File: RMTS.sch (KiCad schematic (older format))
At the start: 54 parts, among them J1 USB_B, J10 CONN_02, J2 Programmer, J3 Screw_Terminal_01x03, J4 Screw_Terminal_01x04, J5 Screw_Terminal_01x02, J6 Screw_Terminal_01x02, J7 Micro_SD_Card_Det_Hirose_DM3AT, J8 CONN_03, J9 CONN_02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

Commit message: Added continuity optocoupler, capacitor pads to loadcell connection
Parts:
- added C17: 0.47uF, Capacitor_SMD:C_0805_2012Metric_Pad1.15x1.40mm_HandSolder, symbol Device:C
- added R11, R12: 500, Resistor_SMD:R_0805_2012Metric_Pad1.15x1.40mm_HandSolder, symbol Device:R_US
- added U5: LTV-817S, Package_DIP:SMDIP-4_W9.53mm, symbol Isolator:LTV-817S
- J10, J9: symbol RMTS-rescue:CONN_02-SparkFun-Connectors -> RMTS-rescue:CONN_02-SparkFun-Connectors-RMTS-rescue
- J8: symbol RMTS-rescue:CONN_03-SparkFun-Connectors -> RMTS-rescue:CONN_03-SparkFun-Connectors-RMTS-rescue
- JP1: symbol RMTS-rescue:XBEE-SparkFun-RF -> RMTS-rescue:XBEE-SparkFun-RF-RMTS-rescue
- U2: symbol RMTS-rescue:MK20DX256VLH7-Mine -> RMTS-rescue:MK20DX256VLH7-Mine-RMTS-rescue
- U3: symbol RMTS-rescue:ADS1219-Mine -> RMTS-rescue:ADS1219-Mine-RMTS-rescue
- U4: symbol RMTS-rescue:MCP6N11-Mine -> RMTS-rescue:MCP6N11-Mine-RMTS-rescue
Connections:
- net labels added: CONT
- wire segments 197 -> 206
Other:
- moved on the sheet: D1, D3, J5, J6, Q1, R9

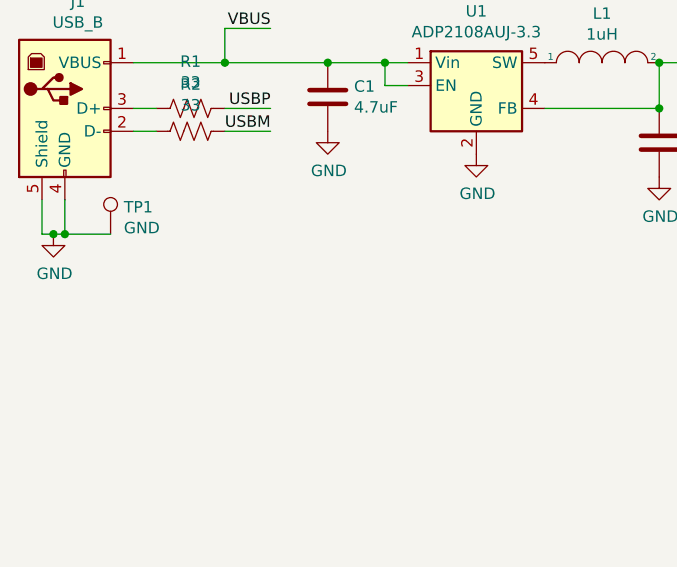
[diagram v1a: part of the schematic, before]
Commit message: Added resistor to avoid battery shutting off
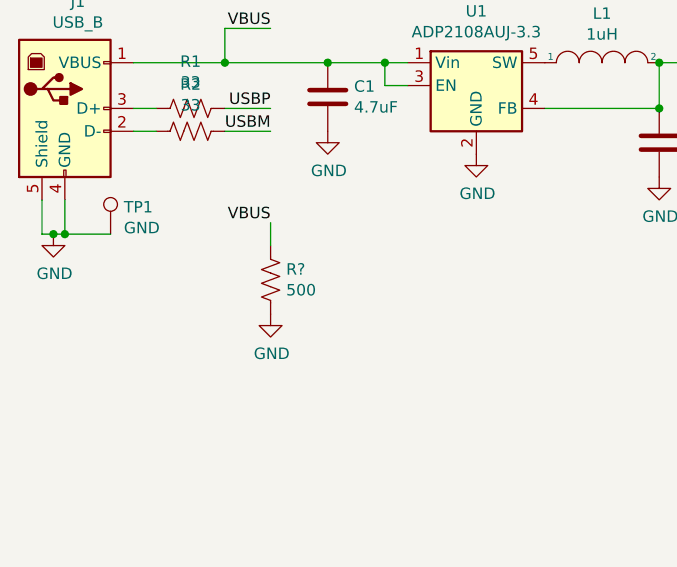
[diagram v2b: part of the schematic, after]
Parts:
- added R?: 500, symbol Device:R_US
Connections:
- net GND: now also R?.2
- net VBUS: now also R?.1
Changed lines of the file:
@@
 Wire Wire Line
 	14100 6600 14400 6600
+$Comp
+L Device:R_US R?
+U 1 1 5E3F0EC8
+P 1900 2200
+F 0 "R?" H 1968 2246 50  0000 L CNN
+F 1 "500" H 1968 2155 50  0000 L CNN
+F 2 "" V 1940 2190 50  0001 C CNN
+F 3 "~" H 1900 2200 50  0001 C CNN
+	1    1900 2200
+	1    0    0    -1
+$EndComp
+$Comp
+L power:GND #PWR?
+U 1 1 5E3F4010
+P 1900 2350
+F 0 "#PWR?" H 1900 2100 50  0001 C CNN
+F 1 "GND" H 1905 2177 50  0000 C CNN
+F 2 "" H 1900 2350 50  0001 C CNN
+F 3 "" H 1900 2350 50  0001 C CNN
+	1    1900 2350
+	1    0    0    -1
+$EndComp
+Text Label 1900 1950 2    50   ~ 0
+VBUS
+Wire Wire Line
+	1900 1950 1900 2050
 $EndSCHEMATC

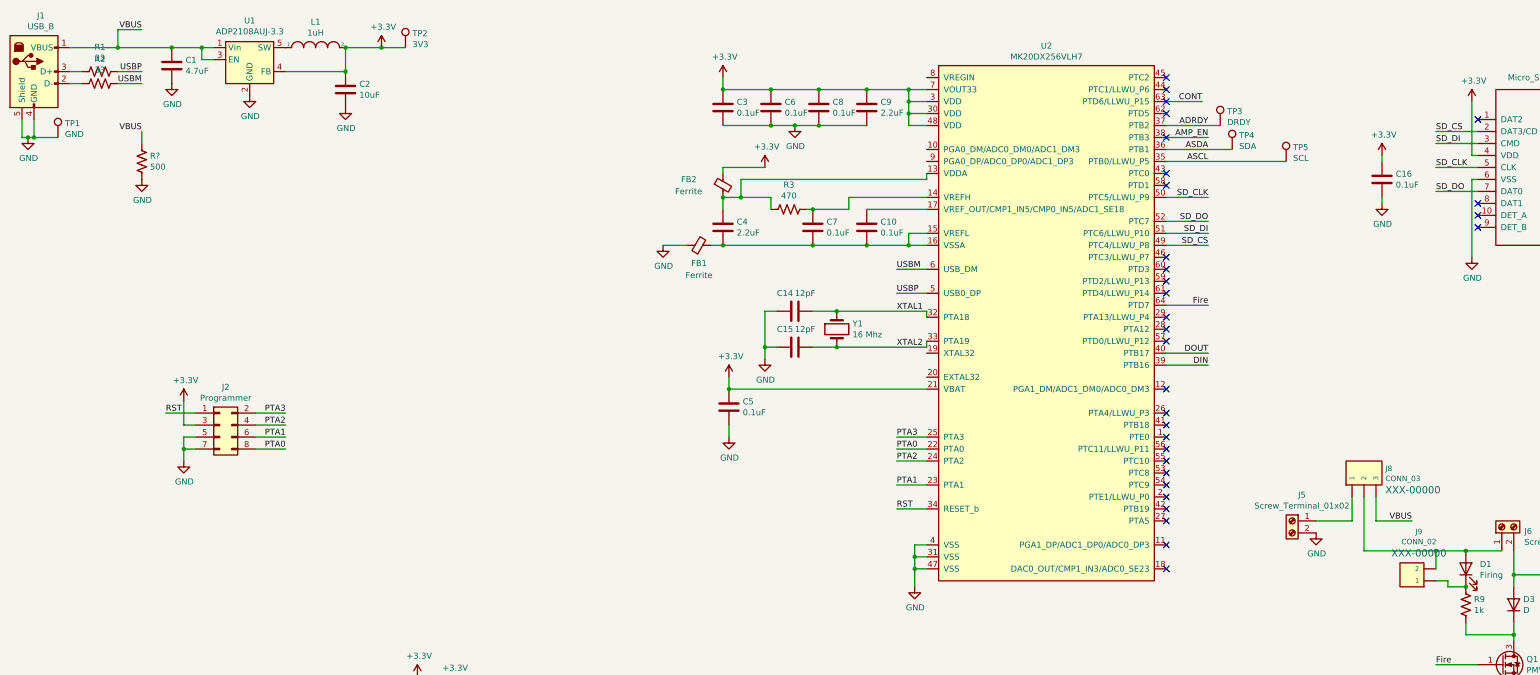
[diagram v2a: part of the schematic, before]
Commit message: Removed USB pyro power jumper
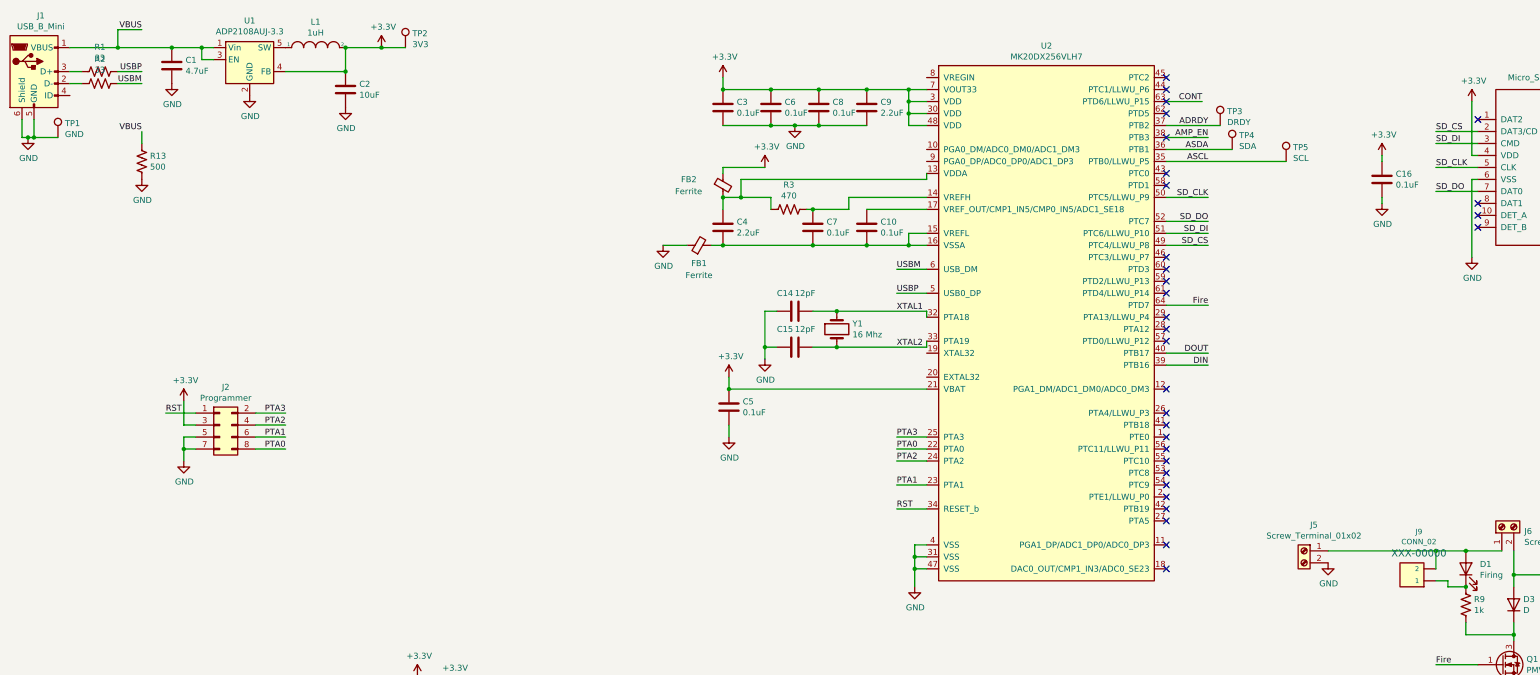
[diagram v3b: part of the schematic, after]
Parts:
- removed J1: USB_B, Connector_USB:USB_B_OST_USB-B1HSxx_Horizontal, symbol Connector:USB_B
- removed J8: CONN_03, Connectors:1X03, symbol RMTS-rescue:CONN_03-SparkFun-Connectors-RMTS-rescue
- added J1: USB_B_Mini, Connector_USB:USB_Mini-B_Lumberg_2486_01_Horizontal, symbol Connector:USB_B_Mini
- R13: renamed from R?; footprint (none) -> Resistor_SMD:R_0805_2012Metric_Pad1.15x1.40mm_HandSolder
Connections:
- net GND: now also J1.5 (GND), J1.6 (Shield)
- net VBUS: now also J1.1 (VBUS)
- net at R1.2: now also J1.3 (D+)
- net at R2.2: now also J1.2 (D-)
- net at D1.2 (A), J6.1 (Pin_1), J9.2: now also J5.1 (Pin_1)
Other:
- moved on the sheet: J5
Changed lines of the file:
@@
 Wire Wire Line
 	13250 5450 12950 5450
-Text Label 12500 5200 2    50   ~ 0
-VBUS
 $Comp
 L Device:LED D2
@@
 L Connector:Screw_Terminal_01x02 J5
 U 1 1 5D6E654F
-P 11500 5200
-F 0 "J5" H 11418 5417 50  0000 C CNN
-F 1 "Screw_Terminal_01x02" H 11418 5326 50  0000 C CNN
-F 2 "Connectors:SCREWTERMINAL-3.5MM-2" H 11500 5200 50  0001 C CNN
-F 3 "~" H 11500 5200 50  0001 C CNN
-	1    11500 5200
+P 11600 5450
+F 0 "J5" H 11518 5667 50  0000 C CNN
+F 1 "Screw_Terminal_01x02" H 11518 5576 50  0000 C CNN
+F 2 "Connectors:SCREWTERMINAL-3.5MM-2" H 11600 5450 50  0001 C CNN
+F 3 "~" H 11600 5450 50  0001 C CNN
+	1    11600 5450
 	-1   0    0    -1
 $EndComp
@@
 L power:GND #PWR0136
 U 1 1 5D6EF1A3
-P 11700 5300
-F 0 "#PWR0136" H 11700 5050 50  0001 C CNN
-F 1 "GND" H 11705 5127 50  0000 C CNN
-F 2 "" H 11700 5300 50  0001 C CNN
-F 3 "" H 11700 5300 50  0001 C CNN
-	1    11700 5300
-	1    0    0    -1
-$EndComp
-$Comp
-L RMTS-rescue:CONN_03-SparkFun-Connectors-RMTS-rescue J8
-U 1 1 5D6FAE37
-P 12000 4900
-F 0 "J8" V 11863 5178 45  0000 L CNN
-F 1 "CONN_03" V 11947 5178 45  0000 L CNN
-F 2 "Connectors:1X03" H 12000 5300 20  0001 C CNN
-F 3 "" H 12000 4900 50  0001 C CNN
-F 4 "XXX-00000" V 12042 5178 60  0000 L CNN "Field4"
-	1    12000 4900
-	0    1    1    0
-$EndComp
-Wire Wire Line
-	12100 5000 12100 5450
-Wire Wire Line
-	12100 5450 12700 5450
-Wire Wire Line
-	12200 5000 12200 5200
-Wire Wire Line
-	12200 5200 12500 5200
-Wire Wire Line
-	11700 5200 12000 5200
-Wire Wire Line
-	12000 5200 12000 5000
+P 11800 5550
+F 0 "#PWR0136" H 11800 5300 50  0001 C CNN
+F 1 "GND" H 11805 5377 50  0000 C CNN
+F 2 "" H 11800 5550 50  0001 C CNN
+F 3 "" H 11800 5550 50  0001 C CNN
+	1    11800 5550
+	1    0    0    -1
+$EndComp
 $Comp
 L Device:C C14
@@
 AMP_EN
 $Comp
-L Connector:USB_B J1
-U 1 1 5D732327
-P 1000 1450
-F 0 "J1" H 1057 1917 50  0000 C CNN
-F 1 "USB_B" H 1057 1826 50  0000 C CNN
-F 2 "Connector_USB:USB_B_OST_USB-B1HSxx_Horizontal" H 1150 1400 50  0001 C CNN
-F 3 " ~" H 1150 1400 50  0001 C CNN
-	1    1000 1450
-	1    0    0    -1
-$EndComp
-$Comp
 L Connector:TestPoint TP3
 U 1 1 5D79BB5E
@@
 	14100 6600 14400 6600
 $Comp
-L Device:R_US R?
+L Device:R_US R13
 U 1 1 5E3F0EC8
 P 1900 2200
-F 0 "R?" H 1968 2246 50  0000 L CNN
+F 0 "R13" H 1968 2246 50  0000 L CNN
 F 1 "500" H 1968 2155 50  0000 L CNN
-F 2 "" V 1940 2190 50  0001 C CNN
+F 2 "Resistor_SMD:R_0805_2012Metric_Pad1.15x1.40mm_HandSolder" V 1940 2190 50  0001 C CNN
 F 3 "~" H 1900 2200 50  0001 C CNN
 	1    1900 2200
@@
 $EndComp
 $Comp
-L power:GND #PWR?
+L power:GND #PWR0145
 U 1 1 5E3F4010
 P 1900 2350
-F 0 "#PWR?" H 1900 2100 50  0001 C CNN
+F 0 "#PWR0145" H 1900 2100 50  0001 C CNN
 F 1 "GND" H 1905 2177 50  0000 C CNN
 F 2 "" H 1900 2350 50  0001 C CNN
@@
 Wire Wire Line
 	1900 1950 1900 2050
+$Comp
+L Connector:USB_B_Mini J1
+U 1 1 5E40F3F8
+P 1000 1450
+F 0 "J1" H 1057 1917 50  0000 C CNN
+F 1 "USB_B_Mini" H 1057 1826 50  0000 C CNN
+F 2 "Connector_USB:USB_Mini-B_Lumberg_2486_01_Horizontal" H 1150 1400 50  0001 C CNN
+F 3 "~" H 1150 1400 50  0001 C CNN
+	1    1000 1450
+	1    0    0    -1
+$EndComp
+Wire Wire Line
+	11800 5450 12700 5450
 $EndSCHEMATC

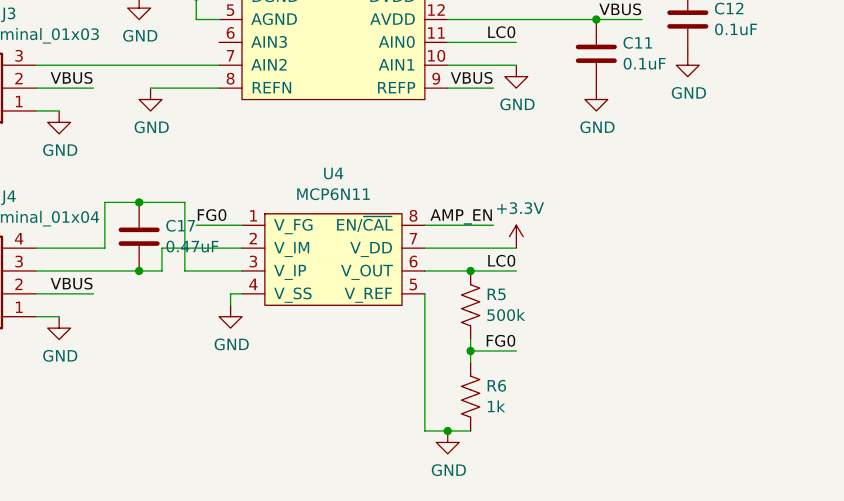
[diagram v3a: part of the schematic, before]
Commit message: Updated amplifier to MCP6N16, incremented revision number
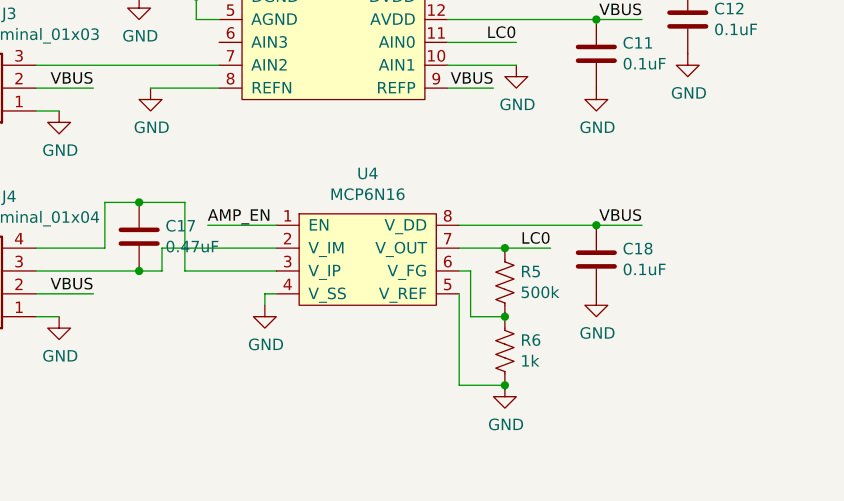
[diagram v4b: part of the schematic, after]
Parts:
- removed U4: MCP6N11, Package_SO:SOIC-8_3.9x4.9mm_P1.27mm, symbol RMTS-rescue:MCP6N11-Mine-RMTS-rescue
- added C18: 0.1uF, Capacitor_SMD:C_0805_2012Metric_Pad1.15x1.40mm_HandSolder, symbol Device:C
- added U4: MCP6N16, Package_SO:MSOP-8_3x3mm_P0.65mm, symbol Mine:MCP6N16
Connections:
- net AMP_EN: now also U4.1 (EN)
- net GND: now also C18.2, U4.4 (V_SS), U4.5 (V_REF)
- net LC0: now also U4.7 (V_OUT)
- net VBUS: now also C18.1, U4.8 (V_DD)
- net at C17.2, J4.3 (Pin_3): now also U4.2 (V_IM)
- net at C17.1, J4.4 (Pin_4): now also U4.3 (V_IP)
- net FG0: no longer names the net of R5.2, R6.1
- net FG0: now also U4.6 (V_FG)
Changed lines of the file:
@@
 	-1   0    0    1
-$EndComp
-$Comp
-L RMTS-rescue:MCP6N11-Mine-RMTS-rescue U4
-U 1 1 5D4392E2
-P 3650 8100
-F 0 "U4" H 3650 8325 50  0000 C CNN
-F 1 "MCP6N11" H 3650 8234 50  0000 C CNN
-F 2 "Package_SO:SOIC-8_3.9x4.9mm_P1.27mm" H 3650 8100 50  0001 C CNN
-F 3 "" H 3650 8100 50  0001 C CNN
-	1    3650 8100
-	1    0    0    -1
 $EndComp
 Wire Wire Line
@@
 VBUS
 Wire Wire Line
-	4050 8200 4450 8200
-Text Label 4350 8100 2    50   ~ 0
-AMP_EN
-Wire Wire Line
-	4050 8100 4350 8100
-Wire Wire Line
-	3250 8400 3200 8400
-$Comp
-L power:GND #PWR0124
-U 1 1 5D49EC97
-P 3200 8450
-F 0 "#PWR0124" H 3200 8200 50  0001 C CNN
-F 1 "GND" H 3205 8277 50  0000 C CNN
-F 2 "" H 3200 8450 50  0001 C CNN
-F 3 "" H 3200 8450 50  0001 C CNN
-	1    3200 8450
-	1    0    0    -1
-$EndComp
-Wire Wire Line
-	3200 8400 3200 8450
-$Comp
-L power:+3.3V #PWR0125
-U 1 1 5D4AF785
-P 4450 8200
-F 0 "#PWR0125" H 4450 8050 50  0001 C CNN
-F 1 "+3.3V" H 4465 8373 50  0000 C CNN
-F 2 "" H 4450 8200 50  0001 C CNN
-F 3 "" H 4450 8200 50  0001 C CNN
-	1    4450 8200
-	1    0    0    -1
-$EndComp
-Text Label 4450 8300 2    50   ~ 0
-LC0
-$Comp
-L Device:R_US R5
-U 1 1 5D4C0410
-P 4250 8450
-F 0 "R5" H 4318 8496 50  0000 L CNN
-F 1 "500k" H 4318 8405 50  0000 L CNN
-F 2 "Resistor_SMD:R_0805_2012Metric_Pad1.15x1.40mm_HandSolder" V 4290 8440 50  0001 C CNN
-F 3 "~" H 4250 8450 50  0001 C CNN
-	1    4250 8450
-	1    0    0    -1
-$EndComp
-$Comp
-L Device:R_US R6
-U 1 1 5D4C1180
-P 4250 8850
-F 0 "R6" H 4318 8896 50  0000 L CNN
-F 1 "1k" H 4318 8805 50  0000 L CNN
-F 2 "Resistor_SMD:R_0805_2012Metric_Pad1.15x1.40mm_HandSolder" V 4290 8840 50  0001 C CNN
-F 3 "~" H 4250 8850 50  0001 C CNN
-	1    4250 8850
-	1    0    0    -1
-$EndComp
-Wire Wire Line
-	4250 8600 4250 8650
-Connection ~ 4250 8650
-Wire Wire Line
-	4250 8650 4250 8700
-Wire Wire Line
-	4050 8400 4050 9000
-Wire Wire Line
-	4050 9000 4150 9000
-Wire Wire Line
-	4250 8650 4450 8650
-Text Label 4450 8650 2    50   ~ 0
-FG0
-Wire Wire Line
-	3250 8100 3050 8100
-Text Label 3050 8100 0    50   ~ 0
-FG0
-Wire Wire Line
 	4150 7300 4450 7300
 Text Label 4450 7300 2    50   ~ 0
 LC0
-$Comp
-L power:GND #PWR0126
-U 1 1 5D52CDAD
-P 4150 9000
-F 0 "#PWR0126" H 4150 8750 50  0001 C CNN
-F 1 "GND" H 4155 8827 50  0000 C CNN
-F 2 "" H 4150 9000 50  0001 C CNN
-F 3 "" H 4150 9000 50  0001 C CNN
-	1    4150 9000
-	1    0    0    -1
-$EndComp
-Connection ~ 4150 9000
-Wire Wire Line
-	4150 9000 4250 9000
 Wire Wire Line
 	4150 7400 4450 7400
@@
 Text Label 12700 2450 0    50   ~ 0
 SD_DO
-Wire Wire Line
-	4050 8300 4250 8300
-Connection ~ 4250 8300
-Wire Wire Line
-	4250 8300 4450 8300
 $Comp
 L power:GND #PWR0133
@@
 Wire Wire Line
 	3000 8000 3000 8300
-Wire Wire Line
-	3000 8300 3250 8300
 Connection ~ 2800 8000
 Wire Wire Line
@@
 Wire Wire Line
 	2900 8300 2900 8200
-Wire Wire Line
-	2900 8200 3250 8200
 Connection ~ 2800 8300
 $Comp
@@
 Wire Wire Line
 	11800 5450 12700 5450
+Wire Wire Line
+	4400 8200 4600 8200
+Connection ~ 4400 8200
+Text Label 4600 8200 2    50   ~ 0
+LC0
+Wire Wire Line
+	4200 8200 4400 8200
+Connection ~ 4400 8500
+Wire Wire Line
+	4250 8300 4200 8300
+Wire Wire Line
+	4250 8500 4250 8300
+Wire Wire Line
+	4400 8500 4250 8500
+$Comp
+L Device:R_US R6
+U 1 1 5E5AA280
+P 4400 8650
+F 0 "R6" H 4468 8696 50  0000 L CNN
+F 1 "1k" H 4468 8605 50  0000 L CNN
+F 2 "Resistor_SMD:R_0805_2012Metric_Pad1.15x1.40mm_HandSolder" V 4440 8640 50  0001 C CNN
+F 3 "~" H 4400 8650 50  0001 C CNN
+	1    4400 8650
+	1    0    0    -1
+$EndComp
+$Comp
+L Device:R_US R5
+U 1 1 5E5A9716
+P 4400 8350
+F 0 "R5" H 4468 8396 50  0000 L CNN
+F 1 "500k" H 4468 8305 50  0000 L CNN
+F 2 "Resistor_SMD:R_0805_2012Metric_Pad1.15x1.40mm_HandSolder" V 4440 8340 50  0001 C CNN
+F 3 "~" H 4400 8350 50  0001 C CNN
+	1    4400 8350
+	1    0    0    -1
+$EndComp
+$Comp
+L power:GND #PWR0124
+U 1 1 5E59AFE5
+P 4400 8800
+F 0 "#PWR0124" H 4400 8550 50  0001 C CNN
+F 1 "GND" H 4405 8627 50  0000 C CNN
+F 2 "" H 4400 8800 50  0001 C CNN
+F 3 "" H 4400 8800 50  0001 C CNN
+	1    4400 8800
+	1    0    0    -1
+$EndComp
+Wire Wire Line
+	3350 8400 3350 8450
+Wire Wire Line
+	3400 8400 3350 8400
+$Comp
+L power:GND #PWR0125
+U 1 1 5E58C5CA
+P 3350 8450
+F 0 "#PWR0125" H 3350 8200 50  0001 C CNN
+F 1 "GND" H 3355 8277 50  0000 C CNN
+F 2 "" H 3350 8450 50  0001 C CNN
+F 3 "" H 3350 8450 50  0001 C CNN
+	1    3350 8450
+	1    0    0    -1
+$EndComp
+Text Label 5000 8100 2    50   ~ 0
+VBUS
+Wire Wire Line
+	3100 8100 3400 8100
+Text Label 3100 8100 0    50   ~ 0
+AMP_EN
+$Comp
+L Mine:MCP6N16 U4
+U 1 1 5E561C9A
+P 3800 8250
+F 0 "U4" H 3800 8625 50  0000 C CNN
+F 1 "MCP6N16" H 3800 8534 50  0000 C CNN
+F 2 "Package_SO:MSOP-8_3x3mm_P0.65mm" H 3800 8250 50  0001 C CNN
+F 3 "" H 3800 8250 50  0001 C CNN
+	1    3800 8250
+	1    0    0    -1
+$EndComp
+Wire Wire Line
+	2900 8200 3400 8200
+Wire Wire Line
+	3000 8300 3400 8300
+Wire Wire Line
+	4400 8800 4200 8800
+Wire Wire Line
+	4200 8800 4200 8400
+Connection ~ 4400 8800
+$Comp
+L Device:C C18
+U 1 1 5E6DE71A
+P 4800 8250
+F 0 "C18" H 4915 8296 50  0000 L CNN
+F 1 "0.1uF" H 4915 8205 50  0000 L CNN
+F 2 "Capacitor_SMD:C_0805_2012Metric_Pad1.15x1.40mm_HandSolder" H 4838 8100 50  0001 C CNN
+F 3 "~" H 4800 8250 50  0001 C CNN
+	1    4800 8250
+	1    0    0    -1
+$EndComp
+Wire Wire Line
+	4200 8100 4800 8100
+Wire Wire Line
+	4800 8100 5000 8100
+Connection ~ 4800 8100
+$Comp
+L power:GND #PWR0126
+U 1 1 5E6F8F4A
+P 4800 8400
+F 0 "#PWR0126" H 4800 8150 50  0001 C CNN
+F 1 "GND" H 4805 8227 50  0000 C CNN
+F 2 "" H 4800 8400 50  0001 C CNN
+F 3 "" H 4800 8400 50  0001 C CNN
+	1    4800 8400
+	1    0    0    -1
+$EndComp
 $EndSCHEMATC
